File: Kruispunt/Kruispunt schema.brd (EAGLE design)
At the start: 100 x 80 mm, 79 parts, among them IC1 74ACT132N, IC2 LM555N, IC3 LM555N, IC4 74AC132N, Q1 BC548, Q10 BC548, Q2 2N3906, Q5 BC548, Q6 2N3906, Q9 BC548

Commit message: Bord en schema + logboek
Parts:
- removed X1: (no value), Kruispunt Library:W237-132
- added C15: 100µF, Kruispunt Library:ELCO-2.5MMLEAD
- added C16: 100nF, Kruispunt Library:ELCO-2.5MMLEAD
- added D15, D16: 1N4004, Kruispunt Library:DO35-7
- added HOLE1, HOLE2, HOLE3, HOLE4: MOUNT-HOLE-4MM, Kruispunt Library:4,0
- added IC5: 786TV, Kruispunt Library:TO220V
- moved IC4 200.3 mm to (92.8, 40.8), flipped to the bottom, turned to 270 degrees
- moved D8 139.2 mm to (29.2, 8.00)
- moved D12 114.2 mm to (29.2, 12.7)
- moved C1 113.1 mm to (38.1, 41.9)
- moved C6 109.7 mm to (20.3, 11.4)
- moved D9 99.4 mm to (29.2, 17.4)
- moved C5 94.4 mm to (5.08, 15.2)
- moved D13 76.5 mm to (79.8, 42.0), turned to 270 degrees
- moved Q5 72.7 mm to (20.3, 5.59)
- moved X5 71.6 mm to (60.7, 4.95), turned to 0 degrees
- moved Q6 67.9 mm to (12.7, 8.89)
- moved Q7 48.9 mm to (29.2, 26.7)
- moved Q8 48.9 mm to (29.2, 21.6)
- moved R26 47.6 mm to (20.3, 19.1)
- moved D14 47.3 mm to (84.8, 42.2), turned to 270 degrees
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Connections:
- new net N$45: C15.+, D15.C, D16.C, IC5.1
- net GND: now also C15.-, C16.-, IC5.2; no longer X1.1
- net VCC: now also C16.+, D16.A, IC5.3; no longer X5.2
- net VCC-LUS: now also D15.A, X5.2; no longer X1.2
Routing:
- net VCC: track 0.00 -> 305.8 mm
- net DIG-IN: track 0.00 -> 211.7 mm
- net N$35: track 0.00 -> 102.5 mm
- net N$44: track 0.00 -> 101.2 mm
- net VCC-LUS: track 0.00 -> 83.8 mm
- net N$33: track 0.00 -> 76.3 mm
- net N$8: track 0.00 -> 62.2 mm
- net N$9: track 0.00 -> 58.2 mm
- net N$20: track 0.00 -> 57.4 mm
- net N$40: track 0.00 -> 52.1 mm
- net N$41: track 0.00 -> 48.2 mm
- net N$32: track 0.00 -> 45.5 mm
- net N$21: track 0.00 -> 44.8 mm
- net N$28: track 0.00 -> 43.1 mm
- net N$31: track 0.00 -> 42.4 mm
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- added copper zone on layer 16, net GND
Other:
- board text added: "24V"
- board text added: "24V - 5V"
- board text added: "Detectielussen"
- board text added: "GND"
- board text added: "Lichtsturing"
- board text added: "Vertaginsschema"

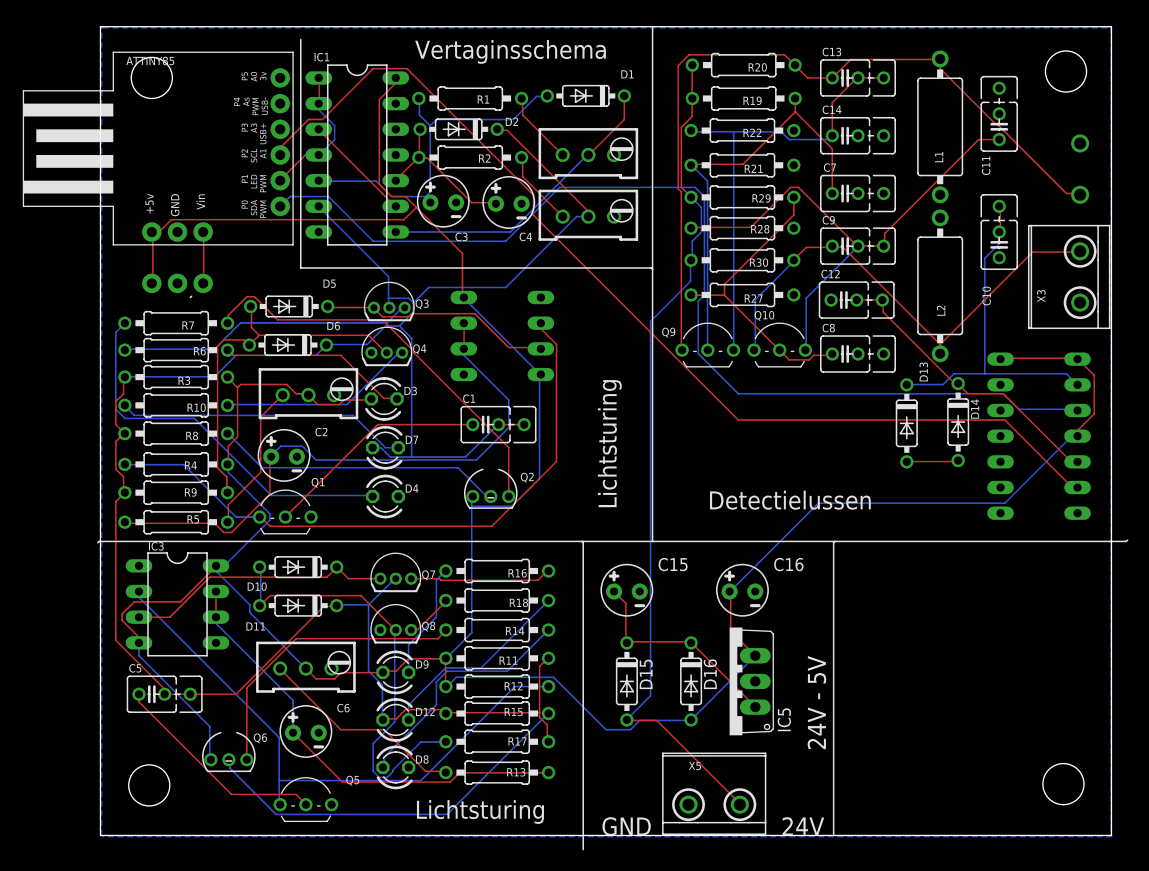
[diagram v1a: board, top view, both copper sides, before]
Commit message: Schema + logboek
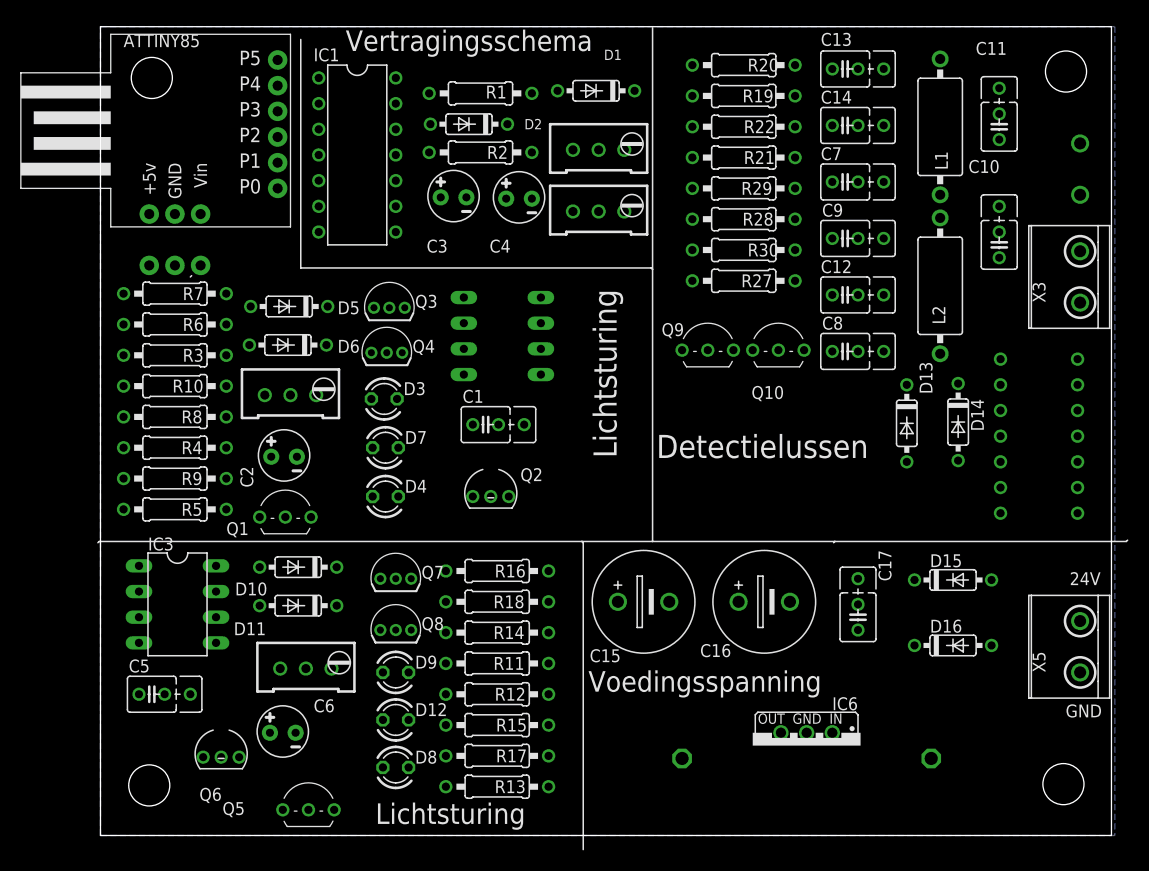
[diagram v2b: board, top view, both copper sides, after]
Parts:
- removed IC5: 786TV, Kruispunt Library:TO220V
- added C17: 100nF, Kruispunt Library:CERAMIC-CAP-C025_050-035X075
- added IC6: (no value), Kruispunt Library:LM78XX-HEATSINK
- C15: value 100µF -> 470µF; device Kruispunt Library:ELCO-2.5MMLEAD -> Kruispunt Library:ELCO-5,0MMLEAD
- C16: value 100nF -> 470µF; device Kruispunt Library:ELCO-2.5MMLEAD -> Kruispunt Library:ELCO-5,0MMLEAD
- D1, D2: value 1N4148DO35-7 -> 1N4148
- moved X5 38.6 mm to (96.3, 19.9), turned to 90 degrees
- moved D15 33.8 mm to (84.3, 26.5), turned to 0 degrees
- moved D16 26.2 mm to (84.3, 20.1), turned to 0 degrees
- moved R7 2.92 mm to (7.37, 54.9)
- moved R6 2.54 mm to (7.37, 51.8)
- moved C16 2.39 mm to (65.7, 24.4)
- moved C6 2.29 mm to (18.0, 11.4)
- moved R3 2.16 mm to (7.37, 48.8)
- moved C15 1.94 mm to (53.7, 24.4)
- moved R10 1.91 mm to (7.37, 45.7)
- moved ATTINY85 1.80 mm to (1.02, 80.5)
- moved R25 1.78 mm to (18.8, 46.1)
- moved R4 1.66 mm to (7.37, 39.6)
- moved R8 1.66 mm to (7.37, 42.7)
- moved R27 1.40 mm to (63.6, 56.1)
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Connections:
- net GND: now also C17.P$1, IC6.GND; no longer IC5.2
- net N$45: now also IC6.IN; no longer IC5.1
- net VCC: now also C17.P$2, C17.P$3, IC6.OUT; no longer IC5.3
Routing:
- net VCC: track 305.8 -> 0.00 mm
- net DIG-IN: track 211.7 -> 0.00 mm
- net N$35: track 102.5 -> 0.00 mm
- net N$44: track 101.2 -> 0.00 mm
- net VCC-LUS: track 83.8 -> 0.00 mm
- net N$33: track 76.3 -> 0.00 mm
- net N$8: track 62.2 -> 0.00 mm
- net N$9: track 58.2 -> 0.00 mm
- net N$20: track 57.4 -> 0.00 mm
- net N$40: track 52.1 -> 0.00 mm
- net N$41: track 48.2 -> 0.00 mm
- net N$32: track 45.5 -> 0.00 mm
- net N$21: track 44.8 -> 0.00 mm
- net N$28: track 43.1 -> 0.00 mm
- net N$31: track 42.4 -> 0.00 mm
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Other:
- board text added: "Vertragingsschema"
- board text added: "Voedingsspanning"
- board text removed: "24V - 5V"
- board text removed: "Vertaginsschema"

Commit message: logboek en schema
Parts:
- D10, D11, D13, D14, D5, D6: value 1N4148DO35-7 -> 1N4148
- IC2, IC3: device Hardware lichtsturing library:DIL08 -> Kruispunt Library:DIL08
- moved D4 2.54 mm to (30.7, 34.8)
- moved D7 2.54 mm to (30.7, 39.6)
- moved D3 2.54 mm to (30.6, 44.5)
- moved IC2 1.98 mm to (41.3, 49.4)
- moved C1 1.98 mm to (39.6, 40.6)
- moved Q2 1.98 mm to (40.1, 33.7)
- moved C6 1.48 mm to (19.3, 10.7)
- moved R25 1.27 mm to (19.8, 46.9)
- moved Q3 1.27 mm to (29.8, 53.5)
- moved Q4 1.27 mm to (29.6, 49.0)
- moved R26 1.27 mm to (19.1, 19.1)
- moved C2 1.27 mm to (19.2, 39.5)
- moved D5 1.27 mm to (19.7, 54.4)
- moved D6 1.27 mm to (19.6, 50.5)
- moved Q1 1.27 mm to (19.3, 34.8)
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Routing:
- net VCC: track 0.00 -> 319.2 mm
- net DIG-IN: track 0.00 -> 215.7 mm
- net N$44: track 0.00 -> 109.8 mm, vias 0 -> 1
- net VCC-LUS: track 0.00 -> 93.6 mm, vias 0 -> 1
- net N$35: track 0.00 -> 89.5 mm
- net N$33: track 0.00 -> 72.2 mm
- net N$20: track 0.00 -> 70.6 mm
- net N$12: track 0.00 -> 65.1 mm, vias 0 -> 1
- net N$41: track 0.00 -> 61.4 mm
- net N$32: track 0.00 -> 61.1 mm
- net N$8: track 0.00 -> 60.3 mm
- net N$40: track 0.00 -> 57.9 mm
- net N$10: track 0.00 -> 51.4 mm, vias 0 -> 1
- net N$9: track 0.00 -> 51.2 mm
- net N$45: track 0.00 -> 50.0 mm
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
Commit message: schema
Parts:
- added C18, C19: 10nF, Kruispunt Library:CERAMIC-CAP-C025_050-035X075
- added PAD1, PAD10, PAD11, PAD12, PAD13, PAD14, PAD15, PAD16, PAD17, PAD2, PAD3, PAD4, PAD5, PAD6, PAD7, PAD8, PAD9: Meetpin, Kruispunt Library:PAD
- added X1: Geel1, Kruispunt Library:90-2
- added X10, X11: (no value), Kruispunt Library:90-2
- added X4: Rood1, Kruispunt Library:90-2
- added X6: Groen1, Kruispunt Library:90-2
- added X7: Geel2, Kruispunt Library:90-2
- added X8: Groen2, Kruispunt Library:90-2
- added X9: Rood2, Kruispunt Library:90-2
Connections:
- new net N$43: C18.P$2, C18.P$3, IC2.5
- new net N$46: ATTINY85.P4, X11.1
- new net N$49: D9.K, R16.1, X9.2
- net DIG-IN: now also D1.C, IC1.8, PAD1.P$1, PAD2.P$1, R24.2, X1.2, X7.2
- net GND: now also C18.P$1, C19.P$1, PAD11.P$1, X10.2, X11.2, X6.1, X8.1
- net N$10: now also PAD17.P$1
- net N$11: now also X6.2
- net N$13: now also PAD12.P$1
- net N$14: now also X4.2
- net N$15: now also PAD8.P$1
- net N$17: now also PAD13.P$1
- net N$18: now also X1.1
- net N$20: now also PAD5.P$1
- net N$22: now also PAD16.P$1
- net N$23: now also X8.2
- net N$25: now also PAD14.P$1
- net N$26: now also ATTINY85.P3, X10.1; no longer D9.K, R16.1
- net N$27: now also PAD6.P$1
- net N$29: now also PAD15.P$1
- net N$30: now also X7.1
- net N$35: now also PAD4.P$1
- net N$38: now also C19.P$2, C19.P$3, IC3.5; no longer D1.C, IC1.8, R24.2
- net N$44: now also PAD3.P$1
- net N$8: now also PAD7.P$1
- net VCC: now also PAD10.P$1, X4.1, X9.1
- net VCC-LUS: now also PAD9.P$1
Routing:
- net VCC: track 319.2 -> 0.00 mm
- net DIG-IN: track 215.7 -> 0.00 mm
- net N$44: track 109.8 -> 0.00 mm, vias 1 -> 0
- net VCC-LUS: track 93.6 -> 0.00 mm, vias 1 -> 0
- net N$35: track 89.5 -> 0.00 mm
- net N$33: track 72.2 -> 0.00 mm
- net N$20: track 70.6 -> 0.00 mm
- net N$12: track 65.1 -> 0.00 mm, vias 1 -> 0
- net N$41: track 61.4 -> 0.00 mm
- net N$32: track 61.1 -> 0.00 mm
- net N$8: track 60.3 -> 0.00 mm
- net N$40: track 57.9 -> 0.00 mm
- net N$10: track 51.4 -> 0.00 mm, vias 1 -> 0
- net N$9: track 51.2 -> 0.00 mm
- net N$45: track 50.0 -> 0.00 mm
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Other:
- board size 100 x 80 mm -> 100 x 100.1 mm
- board text added: "Lichtsturing 1"
- board text added: "Lichtsturing 2"
- board text removed: "Lichtsturing"

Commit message: schema
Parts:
- removed X7: Geel2, Kruispunt Library:90-2
- removed X8: Groen2, Kruispunt Library:90-2
- removed X9: Rood2, Kruispunt Library:90-2
- added X12, X13, X14: (no value), Kruispunt Library:W237-132
- X1: value Geel1 -> (none); device Kruispunt Library:90-2 -> Kruispunt Library:W237-132
- X10, X11: device Kruispunt Library:90-2 -> Kruispunt Library:W237-132
- X4: value Rood1 -> (none); device Kruispunt Library:90-2 -> Kruispunt Library:W237-132
- X6: value Groen1 -> (none); device Kruispunt Library:90-2 -> Kruispunt Library:W237-132
- moved X1 105.9 mm to (-119.7, -96.1)
- moved X6 98.0 mm to (-130.0, -96.1)
- moved X4 65.9 mm to (-88.7, -96.1)
- moved X11 1.33 mm to (-78.4, -96.1)
- moved X10 1.24 mm to (-68.1, -96.1)
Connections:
- net DIG-IN: now also X13.1, X6.1; no longer X1.2, X7.2
- net GND: now also X10.1, X11.1, X12.2, X14.2; no longer X10.2, X11.2, X6.1, X8.1
- net N$11: now also X12.1; no longer X6.2
- net N$14: now also X4.1; no longer X4.2
- net N$18: now also X13.2; no longer X1.1
- net N$23: now also X14.1; no longer X8.2
- net N$26: now also X10.2; no longer X10.1
- net N$30: now also X6.2; no longer X7.1
- net N$46: now also X11.2; no longer X11.1
- net N$49: now also X1.1; no longer X9.2
- net VCC: now also X1.2, X4.2; no longer X4.1, X9.1
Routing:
- removed copper zone on layer 16, net GND

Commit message: jy
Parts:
- moved X10 177.2 mm to (89.6, -15.4)
- moved X12 177.2 mm to (58.7, -15.4)
- moved X1 177.2 mm to (38.0, -15.4)
- moved X11 177.2 mm to (79.3, -15.4)
- moved X13 177.2 mm to (48.4, -15.4)
- moved X14 177.2 mm to (17.4, -15.4)
- moved X4 177.2 mm to (69.0, -15.4)
- moved X6 177.2 mm to (27.7, -15.4)

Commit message: Schema en ppt
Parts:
- X1: value (none) -> Rood2
- X10: value (none) -> Voetgagnersknop1
- X11: value (none) -> Voetgangersknop2
- X12: value (none) -> Groen1
- X13: value (none) -> Geel1
- X14: value (none) -> Groen2
- X4: value (none) -> Rood1
- X6: value (none) -> Geel2
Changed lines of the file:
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@@
 <attribute name="VALUE" x="-7.366" y="-99.314" size="1.27" layer="27"/>
 </element>
-<element name="X10" library="Kruispunt Library" package="W237-132" value="" x="89.60759375" y="-15.433921875" smashed="yes">
+<element name="X10" library="Kruispunt Library" package="W237-132" value="Voetgagnersknop1" x="89.60759375" y="-15.433921875" smashed="yes">
 <attribute name="MF" value="" x="89.60759375" y="-15.433921875" size="1.778" layer="27" display="off"/>
 <attribute name="MPN" value="" x="89.60759375" y="-15.433921875" size="1.778" layer="27" display="off"/>
@@
 <attribute name="VALUE" x="85.79759375" y="-21.148921875" size="1.27" layer="27" ratio="10"/>
 </element>
-<element name="X11" library="Kruispunt Library" package="W237-132" value="" x="79.29519375" y="-15.433921875" smashed="yes">
+<element name="X11" library="Kruispunt Library" package="W237-132" value="Voetgangersknop2" x="79.29519375" y="-15.433921875" smashed="yes">
 <attribute name="MF" value="" x="79.29519375" y="-15.433921875" size="1.778" layer="27" display="off"/>
 <attribute name="MPN" value="" x="79.29519375" y="-15.433921875" size="1.778" layer="27" display="off"/>
@@
 <attribute name="VALUE" x="75.48519375" y="-21.148921875" size="1.27" layer="27" ratio="10"/>
 </element>
-<element name="X4" library="Kruispunt Library" package="W237-132" value="" x="68.98279375" y="-15.433921875" smashed="yes">
+<element name="X4" library="Kruispunt Library" package="W237-132" value="Rood1" x="68.98279375" y="-15.433921875" smashed="yes">
 <attribute name="MF" value="" x="68.98279375" y="-15.433921875" size="1.778" layer="27" display="off"/>
 <attribute name="MPN" value="" x="68.98279375" y="-15.433921875" size="1.778" layer="27" display="off"/>
@@
 <attribute name="VALUE" x="65.17279375" y="-21.148921875" size="1.27" layer="27" ratio="10"/>
 </element>
-<element name="X12" library="Kruispunt Library" package="W237-132" value="" x="58.67039375" y="-15.433921875" smashed="yes">
+<element name="X12" library="Kruispunt Library" package="W237-132" value="Groen1" x="58.67039375" y="-15.433921875" smashed="yes">
 <attribute name="MF" value="" x="58.67039375" y="-15.433921875" size="1.778" layer="27" display="off"/>
 <attribute name="MPN" value="" x="58.67039375" y="-15.433921875" size="1.778" layer="27" display="off"/>
@@
 <attribute name="VALUE" x="54.86039375" y="-21.148921875" size="1.27" layer="27" ratio="10"/>
 </element>
-<element name="X13" library="Kruispunt Library" package="W237-132" value="" x="48.35799375" y="-15.433921875" smashed="yes">
+<element name="X13" library="Kruispunt Library" package="W237-132" value="Geel1" x="48.35799375" y="-15.433921875" smashed="yes">
 <attribute name="MF" value="" x="48.35799375" y="-15.433921875" size="1.778" layer="27" display="off"/>
 <attribute name="MPN" value="" x="48.35799375" y="-15.433921875" size="1.778" layer="27" display="off"/>
@@
 <attribute name="VALUE" x="44.54799375" y="-21.148921875" size="1.27" layer="27" ratio="10"/>
 </element>
-<element name="X1" library="Kruispunt Library" package="W237-132" value="" x="38.04559375" y="-15.433921875" smashed="yes">
+<element name="X1" library="Kruispunt Library" package="W237-132" value="Rood2" x="38.04559375" y="-15.433921875" smashed="yes">
 <attribute name="MF" value="" x="38.04559375" y="-15.433921875" size="1.778" layer="27" display="off"/>
 <attribute name="MPN" value="" x="38.04559375" y="-15.433921875" size="1.778" layer="27" display="off"/>
@@
 <attribute name="VALUE" x="34.23559375" y="-21.148921875" size="1.27" layer="27" ratio="10"/>
 </element>
-<element name="X6" library="Kruispunt Library" package="W237-132" value="" x="27.73319375" y="-15.433921875" smashed="yes">
+<element name="X6" library="Kruispunt Library" package="W237-132" value="Geel2" x="27.73319375" y="-15.433921875" smashed="yes">
 <attribute name="MF" value="" x="27.73319375" y="-15.433921875" size="1.778" layer="27" display="off"/>
 <attribute name="MPN" value="" x="27.73319375" y="-15.433921875" size="1.778" layer="27" display="off"/>
@@
 <attribute name="VALUE" x="23.92319375" y="-21.148921875" size="1.27" layer="27" ratio="10"/>
 </element>
-<element name="X14" library="Kruispunt Library" package="W237-132" value="" x="17.42079375" y="-15.433921875" smashed="yes">
+<element name="X14" library="Kruispunt Library" package="W237-132" value="Groen2" x="17.42079375" y="-15.433921875" smashed="yes">
 <attribute name="MF" value="" x="17.42079375" y="-15.433921875" size="1.778" layer="27" display="off"/>
 <attribute name="MPN" value="" x="17.42079375" y="-15.433921875" size="1.778" layer="27" display="off"/>

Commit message: Schema, gerber, logboek
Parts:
- X11: value Voetgangersknop2 -> Voetgangersknop 2 en 1
- moved PAD17 143.7 mm to (48.4, 33.4)
- moved PAD12 138.8 mm to (47.7, 53.8)
- moved PAD13 133.8 mm to (47.6, 43.4)
- moved PAD9 129.1 mm to (92.3, 26.5)
- moved PAD8 113.3 mm to (26.6, 54.4)
- moved PAD15 98.9 mm to (37.4, -0.42)
- moved PAD16 95.5 mm to (13.9, -1.65)
- moved PAD4 94.3 mm to (14.4, 58.0)
- moved PAD14 90.5 mm to (27.4, -0.34)
- moved PAD7 90.1 mm to (23.4, 36.2)
- moved PAD3 88.5 mm to (2.22, 58.8)
- moved PAD10 76.2 mm to (45.5, -6.68)
- moved PAD11 69.8 mm to (24.6, -6.23)
- moved PAD1 65.9 mm to (61.1, -6.91)
- moved PAD6 61.6 mm to (3.76, 16.4)
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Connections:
- removed net DIG-IN: C1.P$2, C1.P$3, C5.P$2, C5.P$3, D1.C, D11.C, D12.A, D2.C, D6.C, D7.A, IC1.6, IC1.8, PAD1.P$1, PAD2.P$1, Q3.2, Q7.2, R11.2, R15.1, R17.2, R23.2, R24.2, R3.1, R8.1, R9.1, X13.1, X6.1
- new net DIG-IN1: C1.P$2, C1.P$3, D1.C, D6.C, D7.A, IC1.8, PAD1.P$1, Q3.2, R24.2, R3.1, R8.1, R9.1, X13.1
- new net DIG-IN2: C5.P$2, C5.P$3, D11.C, D12.A, D2.C, IC1.6, PAD2.P$1, Q7.2, R11.2, R15.1, R17.2, R23.2, X6.1
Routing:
- net VCC: track 0.00 -> 409.3 mm
- net DIG-IN1: track 0.00 -> 198.0 mm, vias 0 -> 1
- net DIG-IN2: track 0.00 -> 184.1 mm
- net N$26: track 0.00 -> 166.4 mm, vias 0 -> 1
- net N$46: track 0.00 -> 155.5 mm, vias 0 -> 1
- net N$44: track 0.00 -> 128.4 mm, vias 0 -> 1
- net N$14: track 0.00 -> 127.0 mm, vias 0 -> 3
- net N$11: track 0.00 -> 122.5 mm, vias 0 -> 2
- net N$18: track 0.00 -> 121.0 mm, vias 0 -> 3
- net VCC-LUS: track 0.00 -> 109.6 mm, vias 0 -> 1
- net N$35: track 0.00 -> 89.5 mm
- net N$43: track 0.00 -> 88.1 mm, vias 0 -> 1
- net N$20: track 0.00 -> 81.3 mm, vias 0 -> 2
- net N$10: track 0.00 -> 77.1 mm, vias 0 -> 1
- net N$33: track 0.00 -> 68.9 mm
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- added copper zone on layer 16, net GND
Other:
- board text added: "+"
- board text added: "Kruispunt V1 Robbe Dierickx 11/01/19"
- board text added: "voetgangers knop 2 & 1"
